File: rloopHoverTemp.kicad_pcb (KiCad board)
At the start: 2 copper layers, 30.5 x 39.4 mm, 26 parts, among them P1 CONN_01X02, P2 CONN_01X02, Q1 Q_NPN_BEC, Q2 Q_NPN_BEC, U1 XTR117, U2 TS305-10C50, U3 LTC2054, U4 XTR117, U5 LTC2054

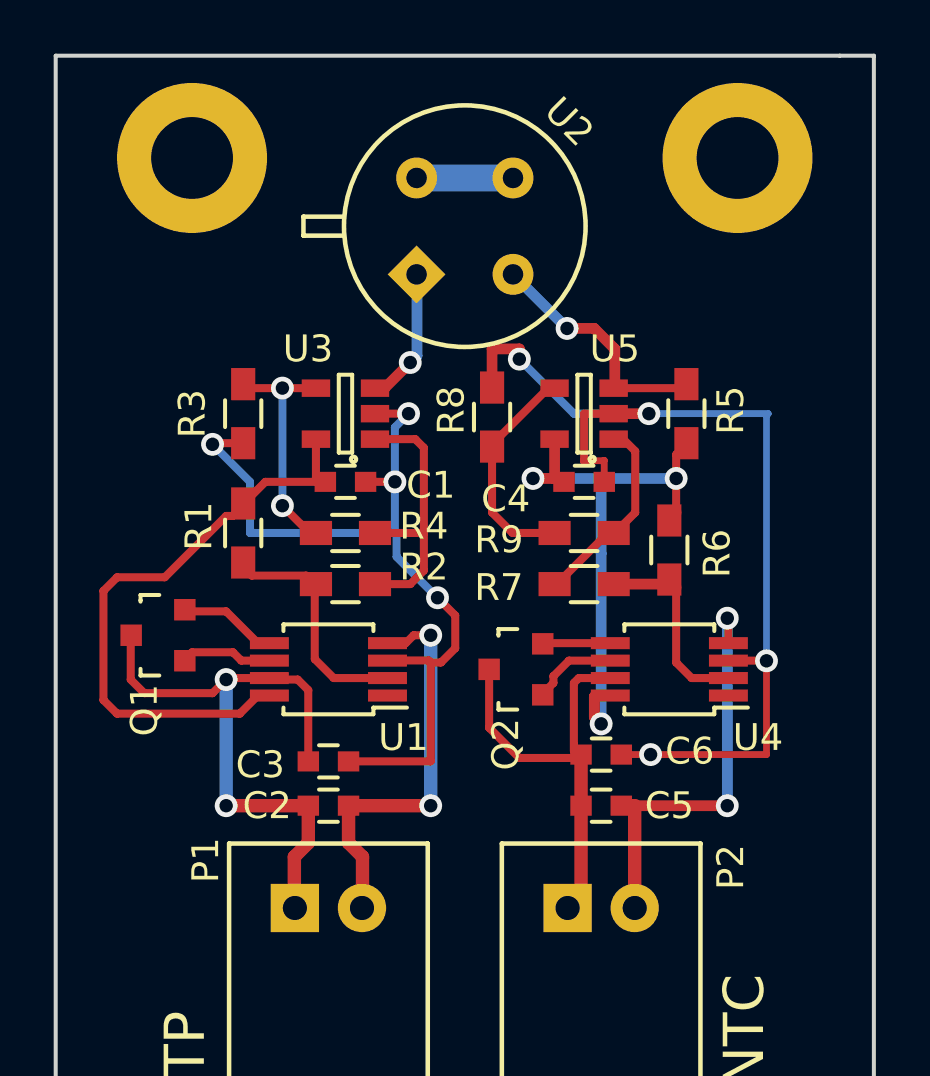
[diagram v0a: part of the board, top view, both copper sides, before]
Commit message: more spacing for 24V, better route, gnd'd mnts
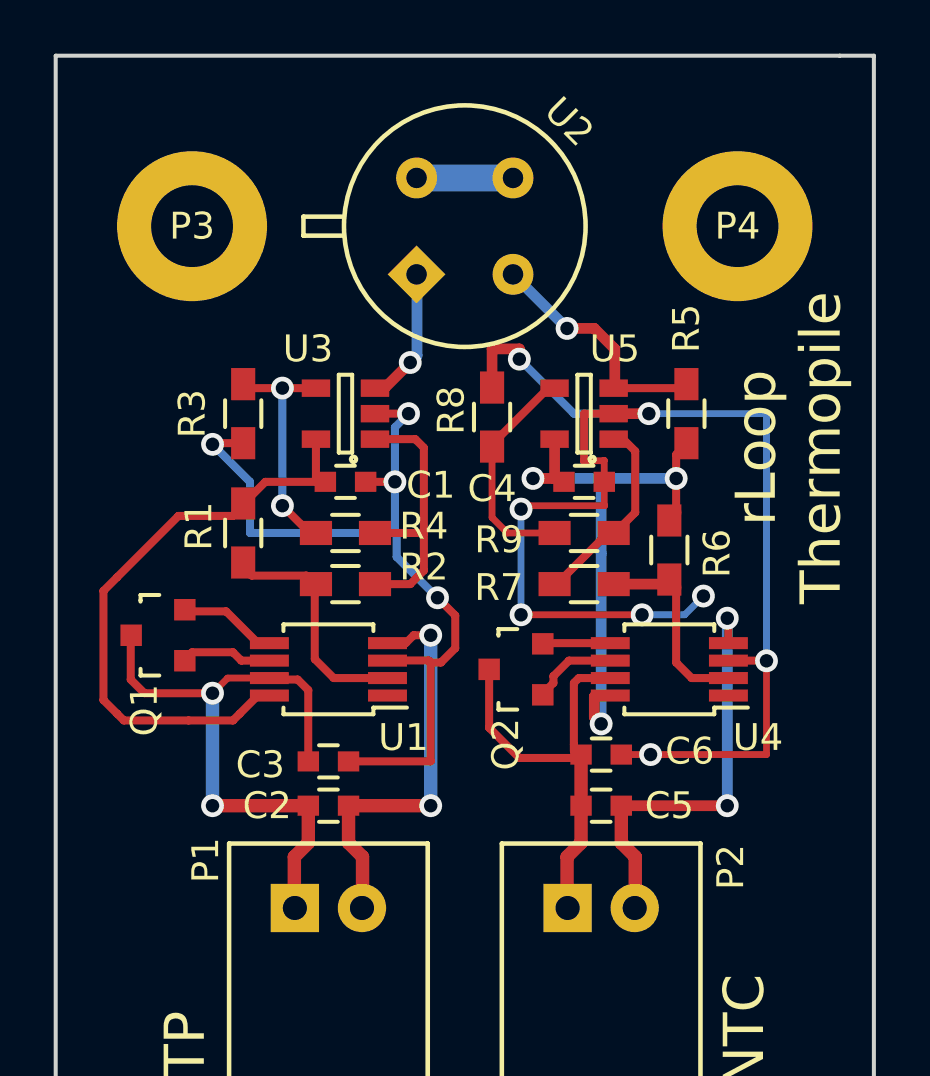
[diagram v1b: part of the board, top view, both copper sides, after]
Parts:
- removed REF** (x2): SCREWPAD-4-40, -footprints:SCREWPAD-4-40
- added P3: CONN_01X01, -footprints:SCREWPAD-4-40, F.Cu at (137.2, 73.7)
- added P4: CONN_01X01, -footprints:SCREWPAD-4-40, F.Cu at (157.5, 73.7)
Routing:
- net GND: track 73.9 -> 89.0 mm, vias 8 -> 12
- net Net-(R8-Pad2): track 8.39 -> 8.92 mm
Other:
- board text added: "rLoop Thermopile"

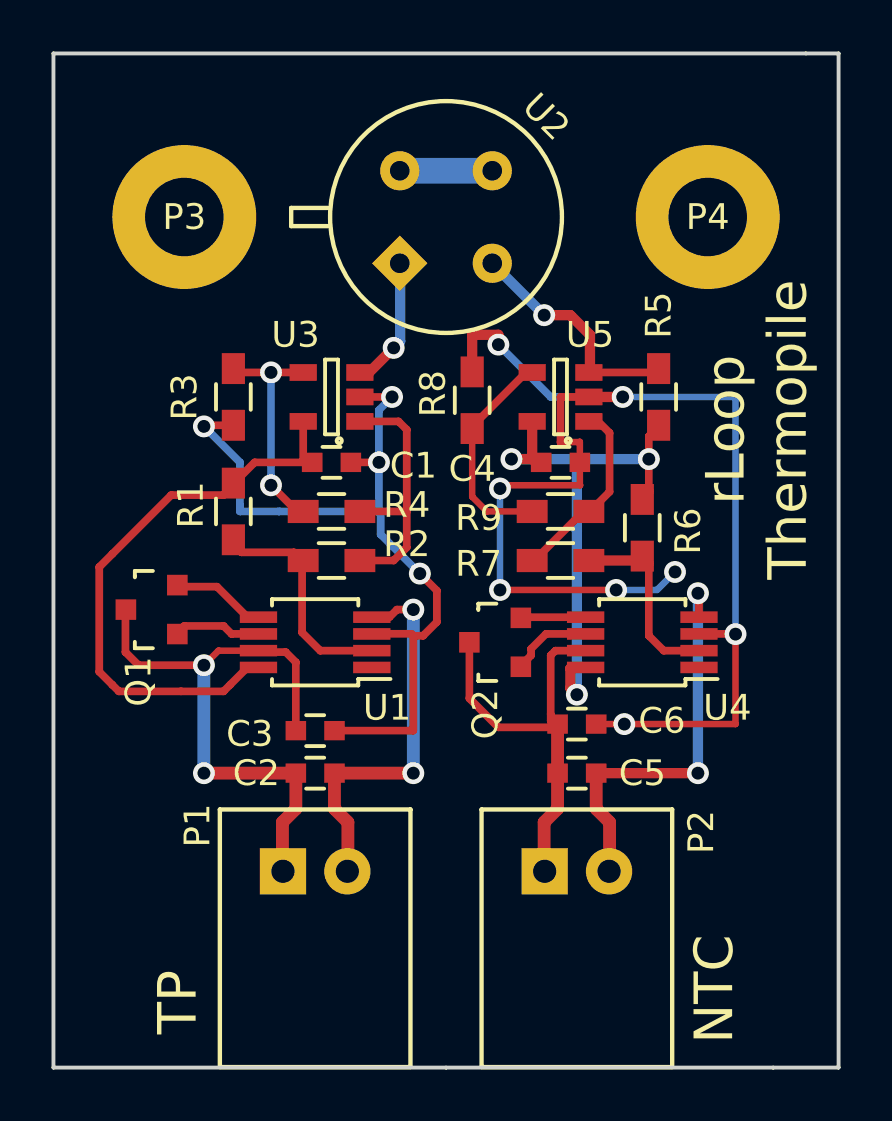
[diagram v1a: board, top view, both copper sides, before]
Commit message: split the grounds
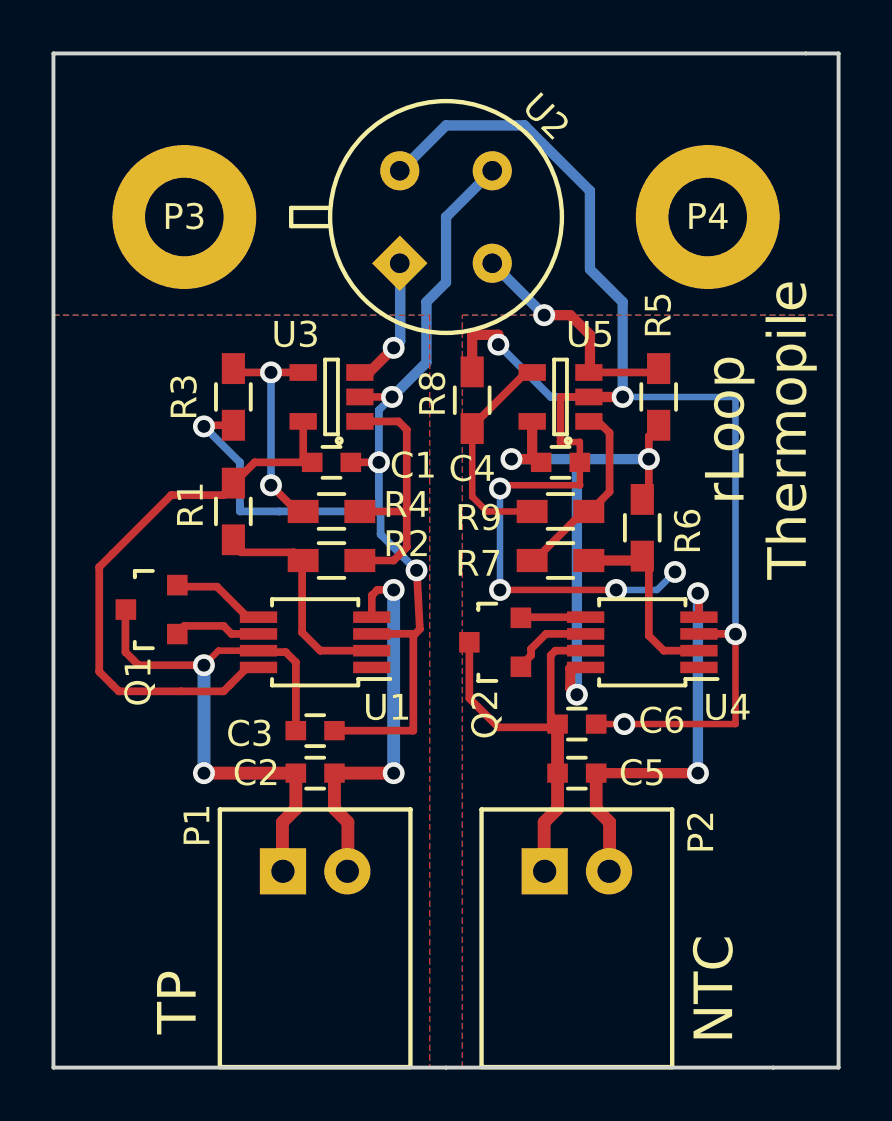
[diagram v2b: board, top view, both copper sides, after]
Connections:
- C1 pad 1: GND -> /GNDA
- C2 pad 1: GND -> /GNDA
- C4 pad 1: GND -> /GNDB
- C5 pad 1: GND -> /GNDB
- P3 pad 1: GND -> Net-(P3-Pad1)
- P4 pad 1: GND -> Net-(P4-Pad1)
- R3 pad 1: GND -> /GNDA
- R8 pad 1: GND -> /GNDB
- U1 pad 3: GND -> /GNDA
- U2 pad 3: GND -> /GNDA
- U2 pad 4: GND -> /GNDB
- U3 pad 2: GND -> /GNDA
- U4 pad 3: GND -> /GNDB
- U5 pad 2: GND -> /GNDB
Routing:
- net GND: track 89.0 -> 0.00 mm, vias 12 -> 0
- net /GNDB: track 0.00 -> 71.1 mm, vias 0 -> 8
- net /GNDA: track 0.00 -> 41.8 mm, vias 0 -> 4
- added copper zone on B.Cu, net /GNDA
- added copper zone on F.Cu, net /GNDA
- added copper zone on B.Cu, net /GNDB
- added copper zone on F.Cu, net /GNDB
- removed copper zone on B.Cu, net GND
- removed copper zone on F.Cu, net GND

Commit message: touchup, put some dimensions on there
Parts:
- moved C2 0.25 mm to (142.2, 93.3)
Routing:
- net /GNDA: track 41.8 -> 38.8 mm
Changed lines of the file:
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@@
     (links 48)
     (no_connects 0)
-    (area 132.004999 67.234999 162.635001 106.755001)
+    (area 131.751667 67.234999 162.888334 107.245001)
     (thickness 1.6)
-    (drawings 11)
-    (tracks 268)
+    (drawings 15)
+    (tracks 267)
     (zones 0)
     (modules 26)
@@
   )
   (setup
-    (last_trace_width 0.3)
+    (last_trace_width 0.254)
     (user_trace_width 0.3)
     (user_trace_width 0.4)
@@
     (pad_to_mask_clearance 0.2)
     (aux_axis_origin 0 0)
-    (grid_origin 153.416 76.454)
+    (grid_origin 147.32 73.66)
     (visible_elements 7FFEFFFF)
     (pcbplotparams
@@
   )
   (module Capacitors_SMD:C_0603 (layer F.Cu)
-    (at 142.24 93.599 180)
+    (at 142.24 93.345 180)
     (descr "Capacitor SMD 0603, reflow soldering, AVX (see smccp.pdf)")
     (tags "capacitor 0603")
@@
     (tags "capacitor 0603")
     (attr smd)
-    (fp_text reference C3 (at -2.54 -1.524) (layer F.SilkS)
+    (fp_text reference C3 (at -2.54 -1.905) (layer F.SilkS)
       (effects (font (size 1 1) (thickness 0.15)))
     )
@@
       (net 22 "Net-(P4-Pad1)"))
   )
+  (dimension 6.35 (width 0.3) (layer Cmts.User)
+    (gr_text "6.350 mm" (at 166.45 70.485 90) (layer Cmts.User)
+      (effects (font (size 1.5 1.5) (thickness 0.3)))
+    )
+    (feature1 (pts (xy 157.48 67.31) (xy 167.8 67.31)))
+    (feature2 (pts (xy 157.48 73.66) (xy 167.8 73.66)))
+    (crossbar (pts (xy 165.1 73.66) (xy 165.1 67.31)))
+    (arrow1a (pts (xy 165.1 67.31) (xy 165.686421 68.436504)))
+    (arrow1b (pts (xy 165.1 67.31) (xy 164.513579 68.436504)))
+    (arrow2a (pts (xy 165.1 73.66) (xy 165.686421 72.533496)))
+    (arrow2b (pts (xy 165.1 73.66) (xy 164.513579 72.533496)))
+  )
+  (dimension 30.48 (width 0.3) (layer Cmts.User)
+    (gr_text "30.480 mm" (at 147.32 110.569999) (layer Cmts.User)
+      (effects (font (size 1.5 1.5) (thickness 0.3)))
+    )
+    (feature1 (pts (xy 162.56 106.68) (xy 162.56 111.919999)))
+    (feature2 (pts (xy 132.08 106.68) (xy 132.08 111.919999)))
+    (crossbar (pts (xy 132.08 109.219999) (xy 162.56 109.219999)))
+    (arrow1a (pts (xy 162.56 109.219999) (xy 161.433496 109.80642)))
+    (arrow1b (pts (xy 162.56 109.219999) (xy 161.433496 108.633578)))
+    (arrow2a (pts (xy 132.08 109.219999) (xy 133.206504 109.80642)))
+    (arrow2b (pts (xy 132.08 109.219999) (xy 133.206504 108.633578)))
+  )
+  (dimension 20.32 (width 0.3) (layer Cmts.User)
+    (gr_text "20.320 mm" (at 147.32 63.42) (layer Cmts.User)
+      (effects (font (size 1.5 1.5) (thickness 0.3)))
+    )
+    (feature1 (pts (xy 157.48 73.66) (xy 157.48 62.07)))
+    (feature2 (pts (xy 137.16 73.66) (xy 137.16 62.07)))
+    (crossbar (pts (xy 137.16 64.77) (xy 157.48 64.77)))
+    (arrow1a (pts (xy 157.48 64.77) (xy 156.353496 65.356421)))
+    (arrow1b (pts (xy 157.48 64.77) (xy 156.353496 64.183579)))
+    (arrow2a (pts (xy 137.16 64.77) (xy 138.286504 65.356421)))
+    (arrow2b (pts (xy 137.16 64.77) (xy 138.286504 64.183579)))
+  )
+  (dimension 39.37 (width 0.3) (layer Cmts.User)
+    (gr_text "39.370 mm" (at 128.19 86.995 270) (layer Cmts.User)
+      (effects (font (size 1.5 1.5) (thickness 0.3)))
+    )
+    (feature1 (pts (xy 132.08 106.68) (xy 126.84 106.68)))
+    (feature2 (pts (xy 132.08 67.31) (xy 126.84 67.31)))
+    (crossbar (pts (xy 129.54 67.31) (xy 129.54 106.68)))
+    (arrow1a (pts (xy 129.54 106.68) (xy 128.953579 105.553496)))
+    (arrow1b (pts (xy 129.54 106.68) (xy 130.126421 105.553496)))
+    (arrow2a (pts (xy 129.54 67.31) (xy 128.953579 68.436504)))
+    (arrow2b (pts (xy 129.54 67.31) (xy 130.126421 68.436504)))
+  )
   (gr_line (start 147.32 96.52) (end 147.32 106.68) (angle 90) (layer Dwgs.User) (width 0.2))
   (gr_text "rLoop\nThermopile" (at 159.385 81.915 90) (layer F.SilkS)
@@
   (segment (start 139.1285 83.947) (end 139.065 83.99) (width 0.3) (layer F.Cu) (net 1))
   (segment (start 140.04 91.145) (end 139.614 91.145) (width 0.3) (layer F.Cu) (net 1))
-  (segment (start 144.44 89.195) (end 144.44 88.351) (width 0.3) (layer F.Cu) (net 2) (status 400000))
+  (segment (start 144.44 89.195) (end 144.44 88.351) (width 0.3) (layer F.Cu) (net 2))
   (via (at 145.288 95.25) (size 0.85) (drill 0.5) (layers F.Cu B.Cu) (net 2))
   (segment (start 145.288 95.25) (end 145.288 88.138) (width 0.5) (layer B.Cu) (net 2))
-  (segment (start 145.288 95.25) (end 142.99 95.25) (width 0.5) (layer F.Cu) (net 2) (status 800000))
+  (segment (start 145.288 95.25) (end 142.99 95.25) (width 0.5) (layer F.Cu) (net 2))
   (via (at 145.288 88.138) (size 0.85) (drill 0.5) (layers F.Cu B.Cu) (net 2))
   (segment (start 144.653 88.138) (end 145.288 88.138) (width 0.3) (layer F.Cu) (net 2))
@@
   (segment (start 134.874 90.551) (end 134.874 89.027) (width 0.3) (layer F.Cu) (net 19))
   (segment (start 138.486 90.495) (end 137.922 91.059) (width 0.254) (layer F.Cu) (net 19))
-  (segment (start 141.49 93.599) (end 141.49 90.944) (width 0.3) (layer F.Cu) (net 19))
+  (segment (start 141.49 93.345) (end 141.49 90.944) (width 0.3) (layer F.Cu) (net 19) (status 10))
   (segment (start 141.097 90.551) (end 140.081 90.551) (width 0.3) (layer F.Cu) (net 19))
   (segment (start 141.49 90.944) (end 141.097 90.551) (width 0.3) (layer F.Cu) (net 19))
@@
   (segment (start 146.177 87.249) (end 146.177 87.376) (width 0.3) (layer F.Cu) (net 23))
   (segment (start 146.304 89.662) (end 146.177 87.249) (width 0.3) (layer F.Cu) (net 23))
-  (segment (start 149.116051 71.863949) (end 147.32 73.66) (width 0.4) (layer B.Cu) (net 23) (status 400000))
+  (segment (start 149.116051 71.863949) (end 147.32 73.66) (width 0.4) (layer B.Cu) (net 23))
   (segment (start 146.558 79.3115) (end 145.2245 80.645) (width 0.4) (layer B.Cu) (net 23))
   (segment (start 146.558 76.962) (end 146.558 79.3115) (width 0.4) (layer B.Cu) (net 23))
   (segment (start 147.32 76.2) (end 146.558 76.962) (width 0.4) (layer B.Cu) (net 23))
   (segment (start 147.32 73.66) (end 147.32 76.2) (width 0.4) (layer B.Cu) (net 23))
-  (segment (start 142.99 93.599) (end 146.05 93.599) (width 0.3) (layer F.Cu) (net 23))
   (segment (start 144.7165 85.0265) (end 144.7165 83.185) (width 0.3) (layer B.Cu) (net 23))
   (segment (start 144.653 85.09) (end 144.7165 85.0265) (width 0.3) (layer B.Cu) (net 23))
@@
   (segment (start 143.975 80.645) (end 145.2245 80.645) (width 0.3) (layer F.Cu) (net 23))
   (via (at 145.2245 80.645) (size 0.85) (drill 0.5) (layers F.Cu B.Cu) (net 23))
-  (segment (start 145.523949 71.863949) (end 145.560051 71.863949) (width 0.4) (layer B.Cu) (net 24) (status C00000))
-  (segment (start 145.560051 71.863949) (end 147.32 70.104) (width 0.4) (layer B.Cu) (net 24) (status 400000))
+  (segment (start 145.523949 71.863949) (end 145.560051 71.863949) (width 0.4) (layer B.Cu) (net 24))
+  (segment (start 145.560051 71.863949) (end 147.32 70.104) (width 0.4) (layer B.Cu) (net 24))
   (segment (start 147.32 70.104) (end 150.368 70.104) (width 0.4) (layer B.Cu) (net 24))
   (segment (start 150.368 70.104) (end 152.908 72.644) (width 0.4) (layer B.Cu) (net 24))

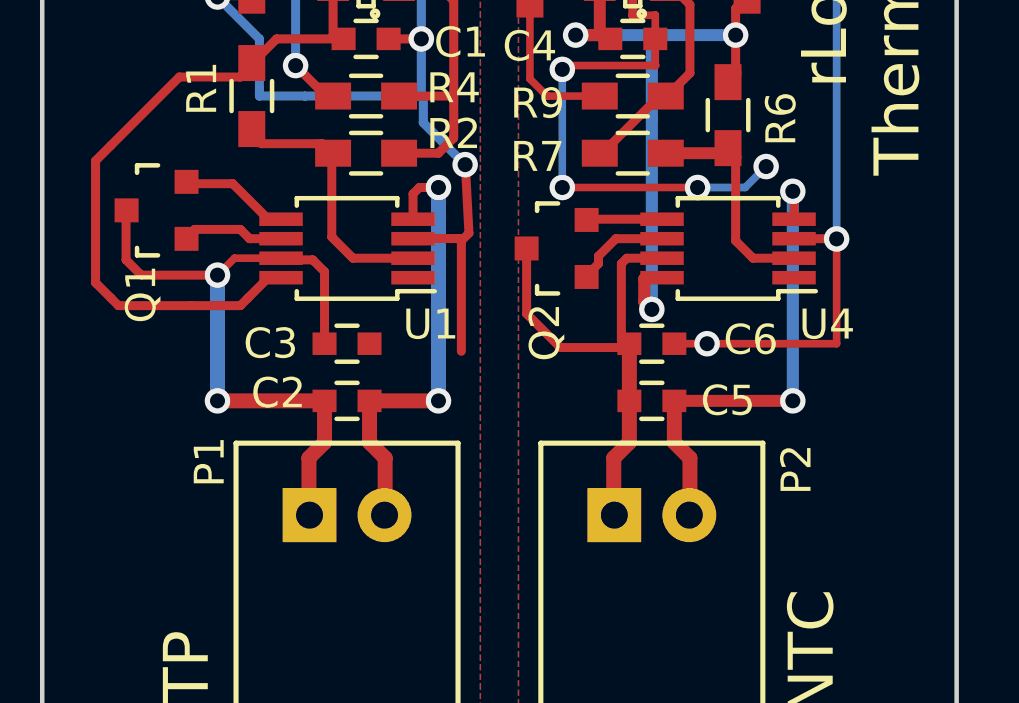
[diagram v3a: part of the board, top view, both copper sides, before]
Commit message: added reverse wiring protection diode
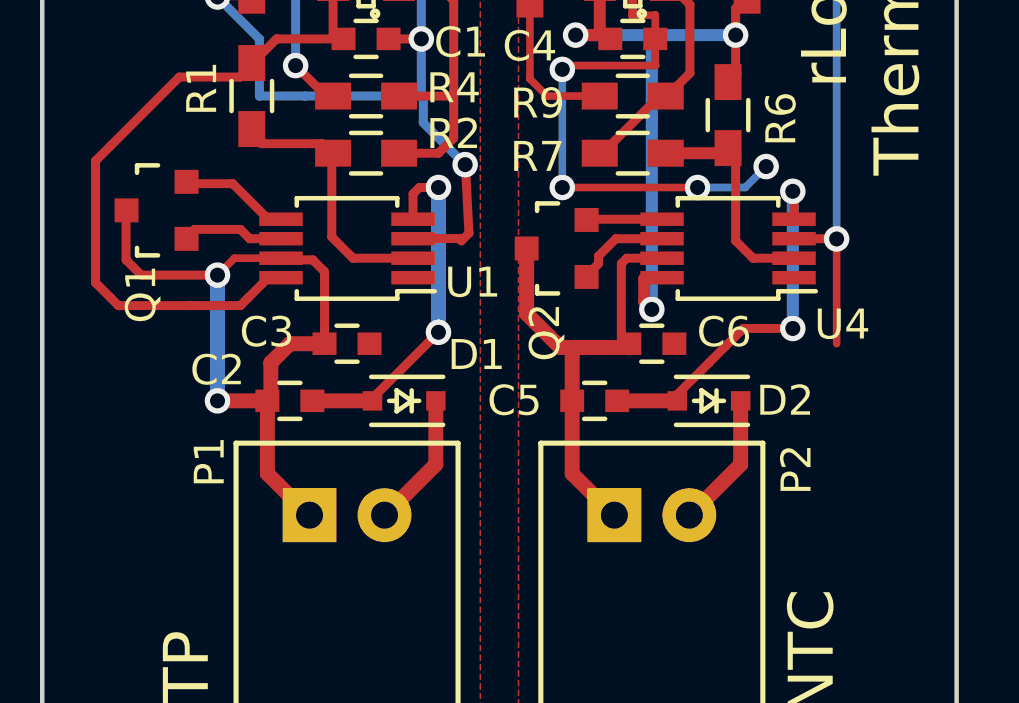
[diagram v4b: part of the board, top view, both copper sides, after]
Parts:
- added D1: D_Small, -footprints:SOD-323, F.Cu at (144.1, 95.2)
- added D2: D_Small, -footprints:SOD-323, F.Cu at (154.3, 95.2)
- moved C3 1.91 mm to (140.3, 95.2)
- moved C6 1.91 mm to (150.5, 95.2)
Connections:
- P1 pad 2: Net-(C3-Pad2) -> Net-(D1-Pad1)
- P2 pad 2: Net-(C6-Pad2) -> Net-(D2-Pad1)
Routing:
- net /GNDB: track 71.1 -> 65.7 mm, vias 8 -> 7
- net Net-(D2-Pad1): track 0.00 -> 4.53 mm
- net Net-(D1-Pad1): track 0.00 -> 4.53 mm
- net /GNDA: track 38.8 -> 35.1 mm
- net Net-(C6-Pad2): track 16.2 -> 12.5 mm
- net Net-(C3-Pad2): track 15.2 -> 12.1 mm
- net /24V_A: track 23.2 -> 25.1 mm
